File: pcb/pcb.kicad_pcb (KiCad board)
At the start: 2 copper layers, 110 x 124 mm, 64 parts, among them J1 AMT0440007DB0000G, J10 Conn_02x10_Odd_Even, J11 Conn_01x03, J12 Conn_01x02, J14 Conn_01x04, J15 Conn_01x10, J16 Conn_01x10, J2 AMT0440007DB0000G, J3 AMT0440007DB0000G, J4 AMT0440007DB0000G, J5 Conn_01x03, J6 Conn_01x03, J7 Conn_01x03, J8 Conn_01x03, J9 Conn_01x03, Q1 IRF9Z34NPBF, Q2 IRF9Z34NPBF, Q3 IRF9Z34NPBF, Q4 IRF9Z34NPBF, Q5 IRF9Z34NPBF, U1 ACS711ELCTR-12AB-T, U2 ACS711ELCTR-12AB-T, U3 ACS711ELCTR-12AB-T, U4 ACS711ELCTR-12AB-T, U5 ACS711ELCTR-12AB-T, U6 TXS0102DCUR, U7 TXS0102DCUR, U8 TXS0102DCUR, U9 NCP718BSNADJT1G

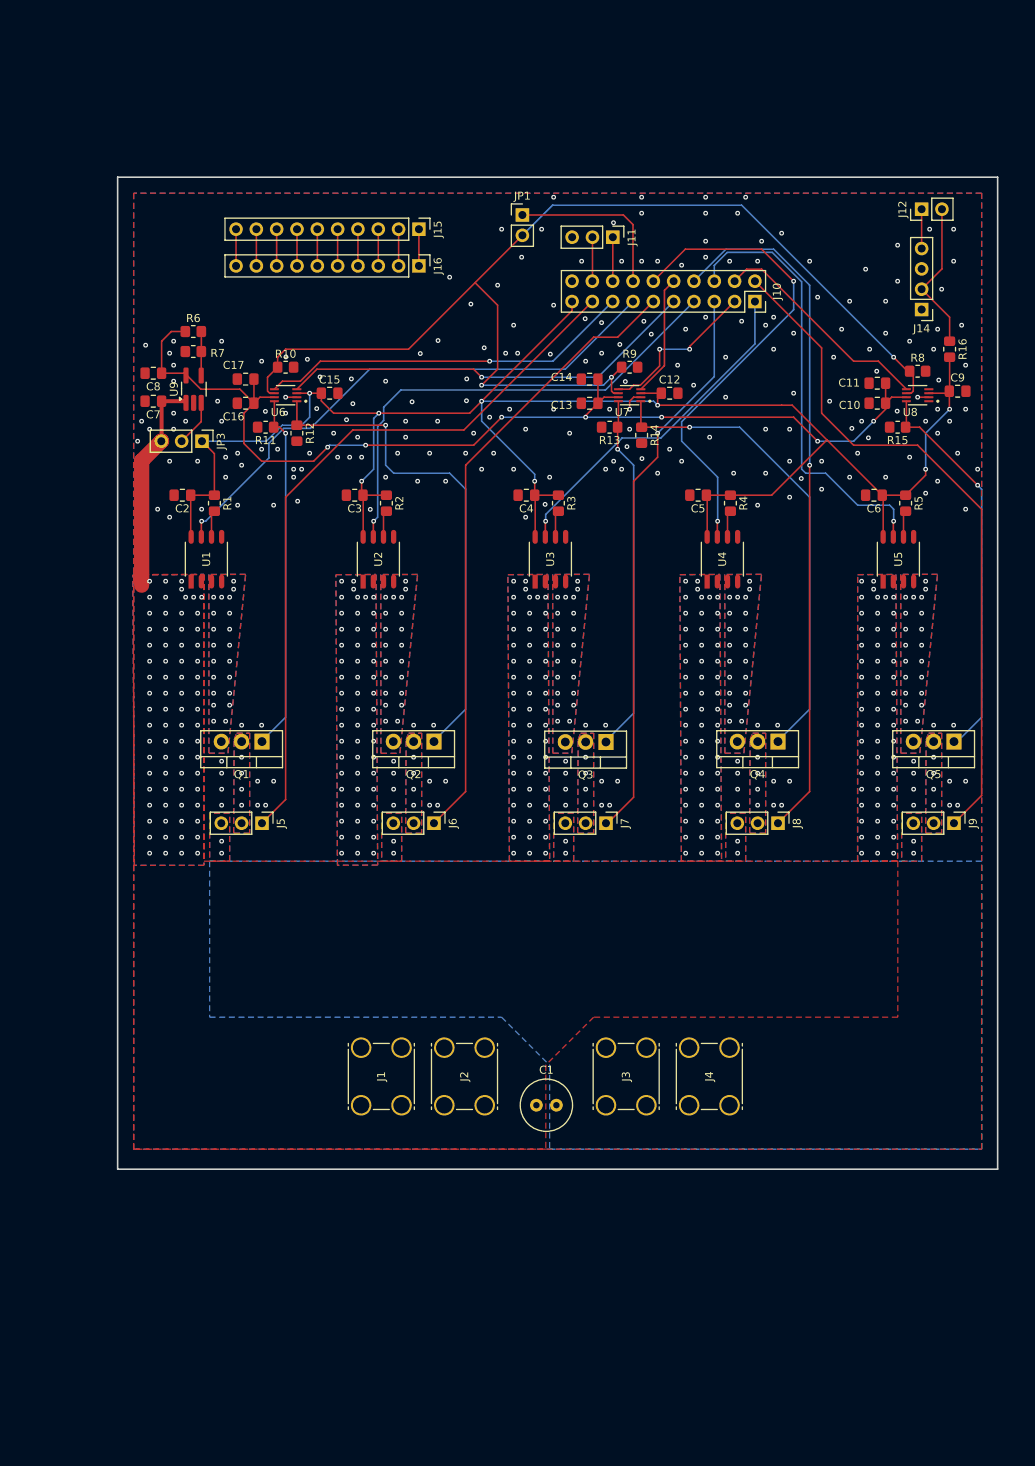
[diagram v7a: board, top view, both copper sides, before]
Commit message: Fix STM32 header footprint and add silkscreen
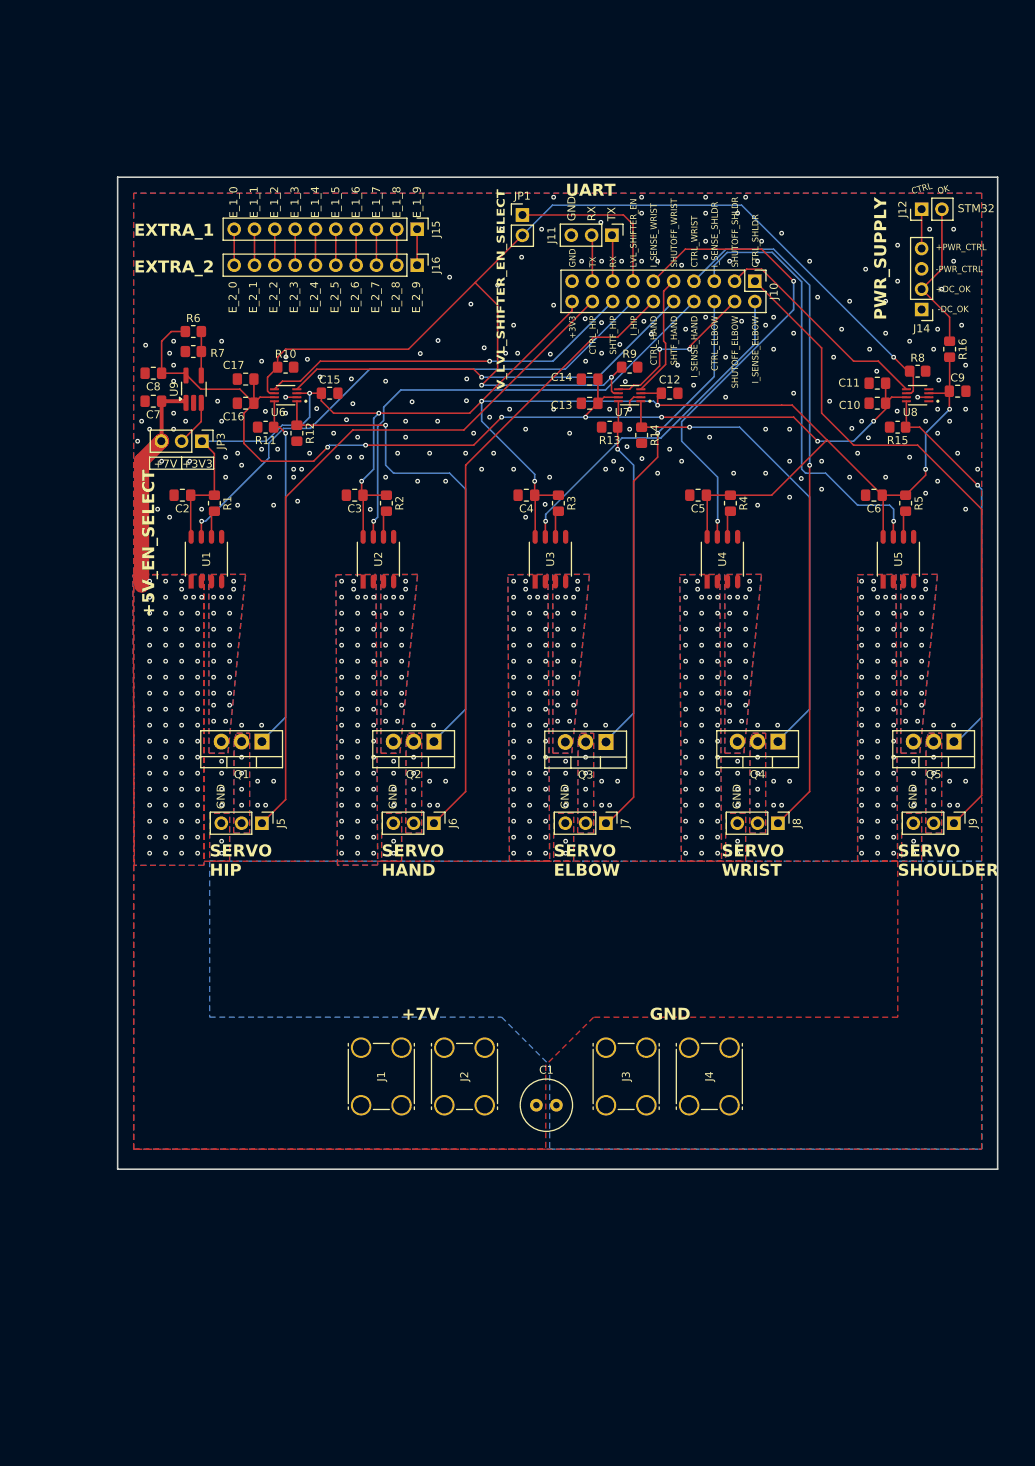
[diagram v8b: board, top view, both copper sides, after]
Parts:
- J10: footprint Connector_PinSocket_2.54mm:PinSocket_2x10_P2.54mm_Vertical -> Connector_PinHeader_2.54mm:PinHeader_2x10_P2.54mm_Vertical
- moved J10 2.54 mm to (171.7, 38.5)
- moved J11 0.27 mm to (153.8, 32.8)
- moved J16 0.25 mm to (129.4, 36.5)
- moved J15 0.23 mm to (129.4, 32.0)
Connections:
- J10 pad 1: I_SENSE_ELBOW -> CTRL_SHOULDER
- J10 pad 10: SHUTOFF_WRIST_L -> SHUTOFF_HAND_L
- J10 pad 11: CTRL_HAND -> I_SENSE_WRIST
- J10 pad 12: I_SENSE_WRIST -> CTRL_HAND
- J10 pad 13: I_SENSE_HIP -> Net-(J10-Pin_13)
- J10 pad 14: Net-(J10-Pin_14) -> I_SENSE_HIP
- J10 pad 15: SHUTOFF_HIP_L -> UART_STM_RX
- J10 pad 16: UART_STM_RX -> SHUTOFF_HIP_L
- J10 pad 17: CTRL_HIP -> UART_STM_TX
- J10 pad 18: UART_STM_TX -> CTRL_HIP
- J10 pad 19: +3V3 -> GNDREF
- J10 pad 2: CTRL_SHOULDER -> I_SENSE_ELBOW
- J10 pad 20: GNDREF -> +3V3
- J10 pad 3: SHUTOFF_ELBOW_L -> SHUTOFF_SHOULDER_L
- J10 pad 4: SHUTOFF_SHOULDER_L -> SHUTOFF_ELBOW_L
- J10 pad 5: CTRL_ELBOW -> I_SENSE_SHOULDER
- J10 pad 6: I_SENSE_SHOULDER -> CTRL_ELBOW
- J10 pad 7: I_SENSE_HAND -> CTRL_WRIST
- J10 pad 8: CTRL_WRIST -> I_SENSE_HAND
- J10 pad 9: SHUTOFF_HAND_L -> SHUTOFF_WRIST_L
- JP1 pad 1: Net-(J10-Pin_14) -> Net-(J10-Pin_13)
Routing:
- net Net-(J10-Pin_14): track 21.4 -> 0.00 mm
- net Net-(J10-Pin_13): track 0.00 -> 21.4 mm
- net GNDREF: vias 252 -> 253
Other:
- board text added: "+3V3"
- board text added: "+5V_EN_SELECT"
- board text added: "+7V"
- board text added: "+DC_OK"
- board text added: "+PWR_CTRL"
- board text added: "-DC_OK"
- board text added: "-PWR_CTRL"
- board text added: "CTRL"
- board text added: "CTRL_ELBOW"
- board text added: "CTRL_HAND"
- board text added: "CTRL_HIP"
- board text added: "CTRL_SHLDR"
- board text added: "CTRL_WRIST"
- board text added: "EXTRA_1"
- board text added: "EXTRA_2"
- board text added: "E_1_0"
- board text added: "E_1_1"
- board text added: "E_1_2"
- board text added: "E_1_3"
- board text added: "E_1_4"
- board text added: "E_1_5"
- board text added: "E_1_6"
- board text added: "E_1_7"
- board text added: "E_1_8"
- board text added: "E_1_9"
- board text added: "E_2_0"
- board text added: "E_2_1"
- board text added: "E_2_2"
- board text added: "E_2_3"
- board text added: "E_2_4"
- board text added: "E_2_5"
- board text added: "E_2_6"
- board text added: "E_2_7"
- board text added: "E_2_8"
- board text added: "E_2_9"
- board text added: "GND"
- board text added: "I_HIP"
- board text added: "I_SENSE_ELBOW"
- board text added: "I_SENSE_HAND"
- board text added: "I_SENSE_HIP"
- board text added: "I_SENSE_SHLDR"
- board text added: "I_SENSE_WRIST"
- board text added: "LVL_SHIFTER_EN"
- board text added: "OK"
- board text added: "PWR_SUPPLY"
- board text added: "RX"
- board text added: "SERVO ELBOW"
- board text added: "SERVO HAND"
- board text added: "SERVO HIP"
- board text added: "SERVO SHOULDER"
- board text added: "SERVO WRIST"
- board text added: "SHTF_HAND"
- board text added: "SHTF_HIP"
- board text added: "SHUTOFF_ELBOW"
- board text added: "SHUTOFF_HAND"
- board text added: "SHUTOFF_HIP"
- board text added: "SHUTOFF_SHLDR"
- board text added: "SHUTOFF_WRIST"
- board text added: "STM32"
- board text added: "TX"
- board text added: "UART"
- board text added: "V_LVL_SHIFTER_EN_SELECT"
